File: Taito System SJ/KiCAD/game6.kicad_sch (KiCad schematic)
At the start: 2 parts, among them U110 74LS174, U24 PAL16L8

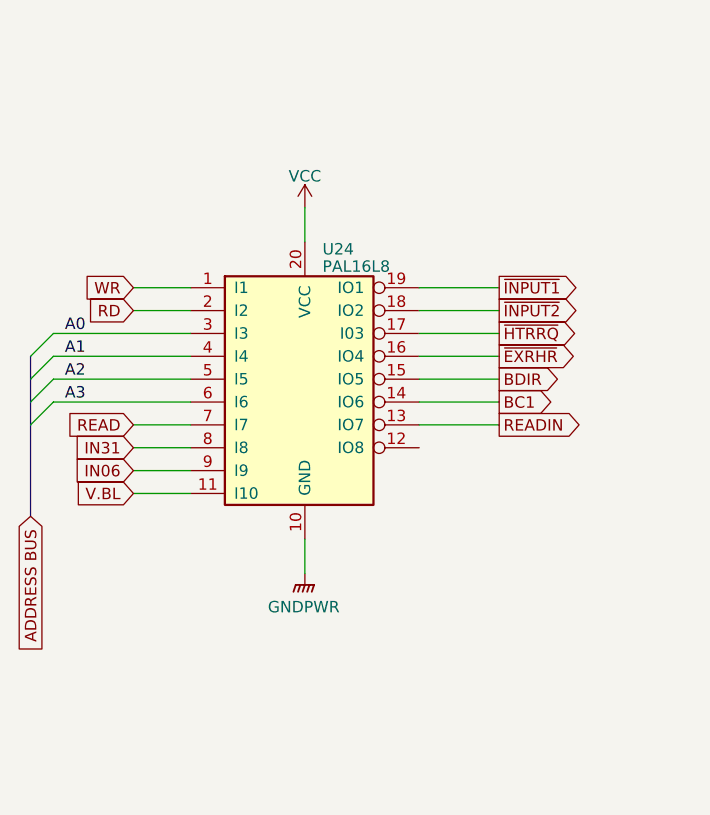
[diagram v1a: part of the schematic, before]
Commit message: Added MCU to Taito SJ Schematics
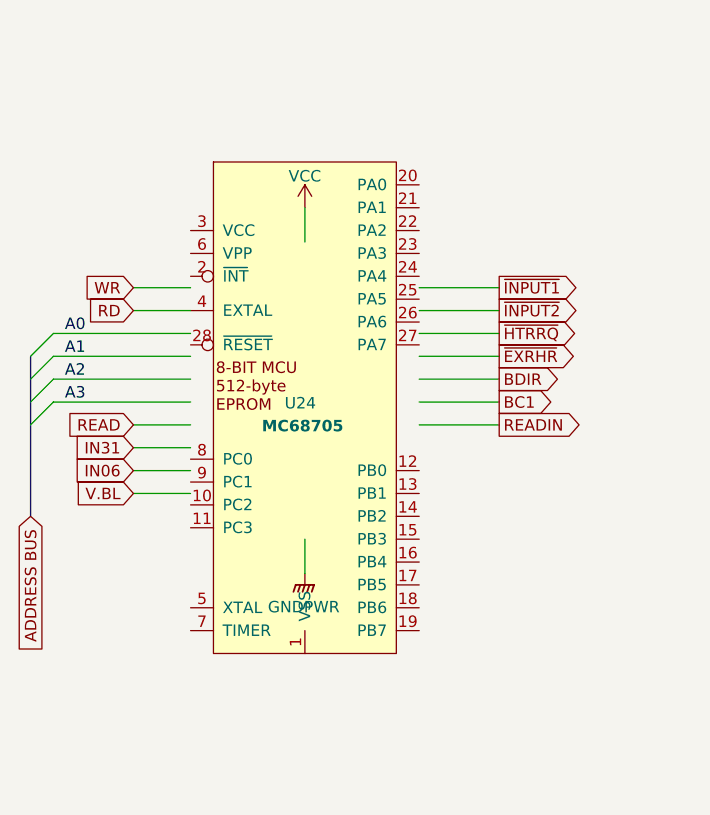
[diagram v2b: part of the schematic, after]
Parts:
- U24: value PAL16L8 -> MC68705
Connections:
- net A0: no longer U24.3 (I3)
- net A1: no longer U24.4 (I4)
- net A2: no longer U24.5 (I5)
- net A3: no longer U24.6 (I6)
- net BC1: no longer U24.14 (IO6)
- net BDIR: no longer U24.15 (IO5)
- net GNDPWR: no longer U24.10 (GND), U24.8 (I8), U24.9 (I9)
- net RD: now also U24.4 (EXTAL); no longer U24.2 (I2)
- net READ: no longer U24.7 (I7)
- net READIN: no longer U24.13 (IO7)
- net V.BL: no longer U24.11 (I10)
- net VCC: no longer U24.20 (VCC)
- net WR: no longer U24.1 (I1)
- net ~{EXRHR}: no longer U24.16 (IO4)
- net ~{HTRRQ}: no longer U24.17 (I03)
- net ~{INPUT1}: no longer U24.19 (IO1)
- net ~{INPUT2}: no longer U24.18 (IO2)

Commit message: Updated Taito SJ Schematics
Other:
- company: (none) -> ANTON GALE
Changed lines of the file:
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@@
 	(generator_version "9.0")
 	(paper "C")
+	(title_block
+		(company "ANTON GALE")
+	)
 	(junction
 		(at 193.04 54.61)
